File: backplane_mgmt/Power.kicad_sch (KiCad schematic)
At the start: 67 parts, among them J304 VIn, Q301 SUD19P06-60, Q302 SUD19P06-60, U301 AZ1117CD-5.0, U302 PTH08T220, U303 INA209, U304 INA209, U305 AT30TS74

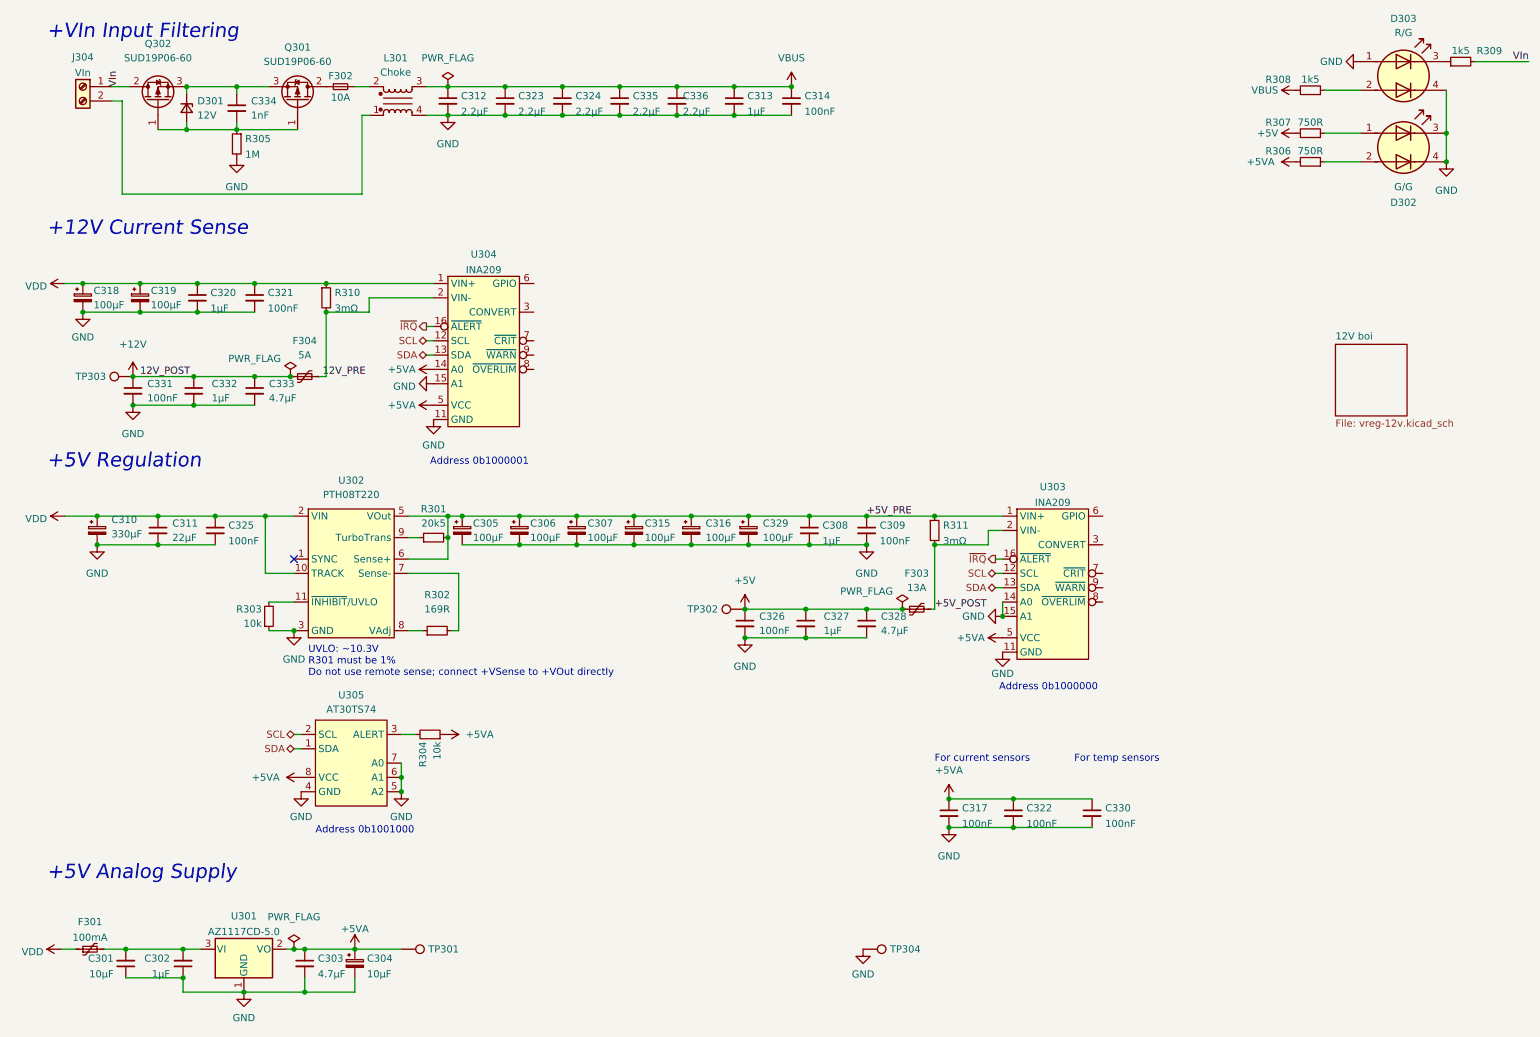
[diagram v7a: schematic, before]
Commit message: Minor layout tweaks across the board
- Added an input for a test clock, and a jumper for sending this clock
  instead of the CPU clock to the clock pins of the expansion cards on
  the backplane boards

- Reworked a bunch of the power supply board

- Minor changes (to consolidate BOMs) on CPU board for some capacitors,
  they were replaced with SMD versions
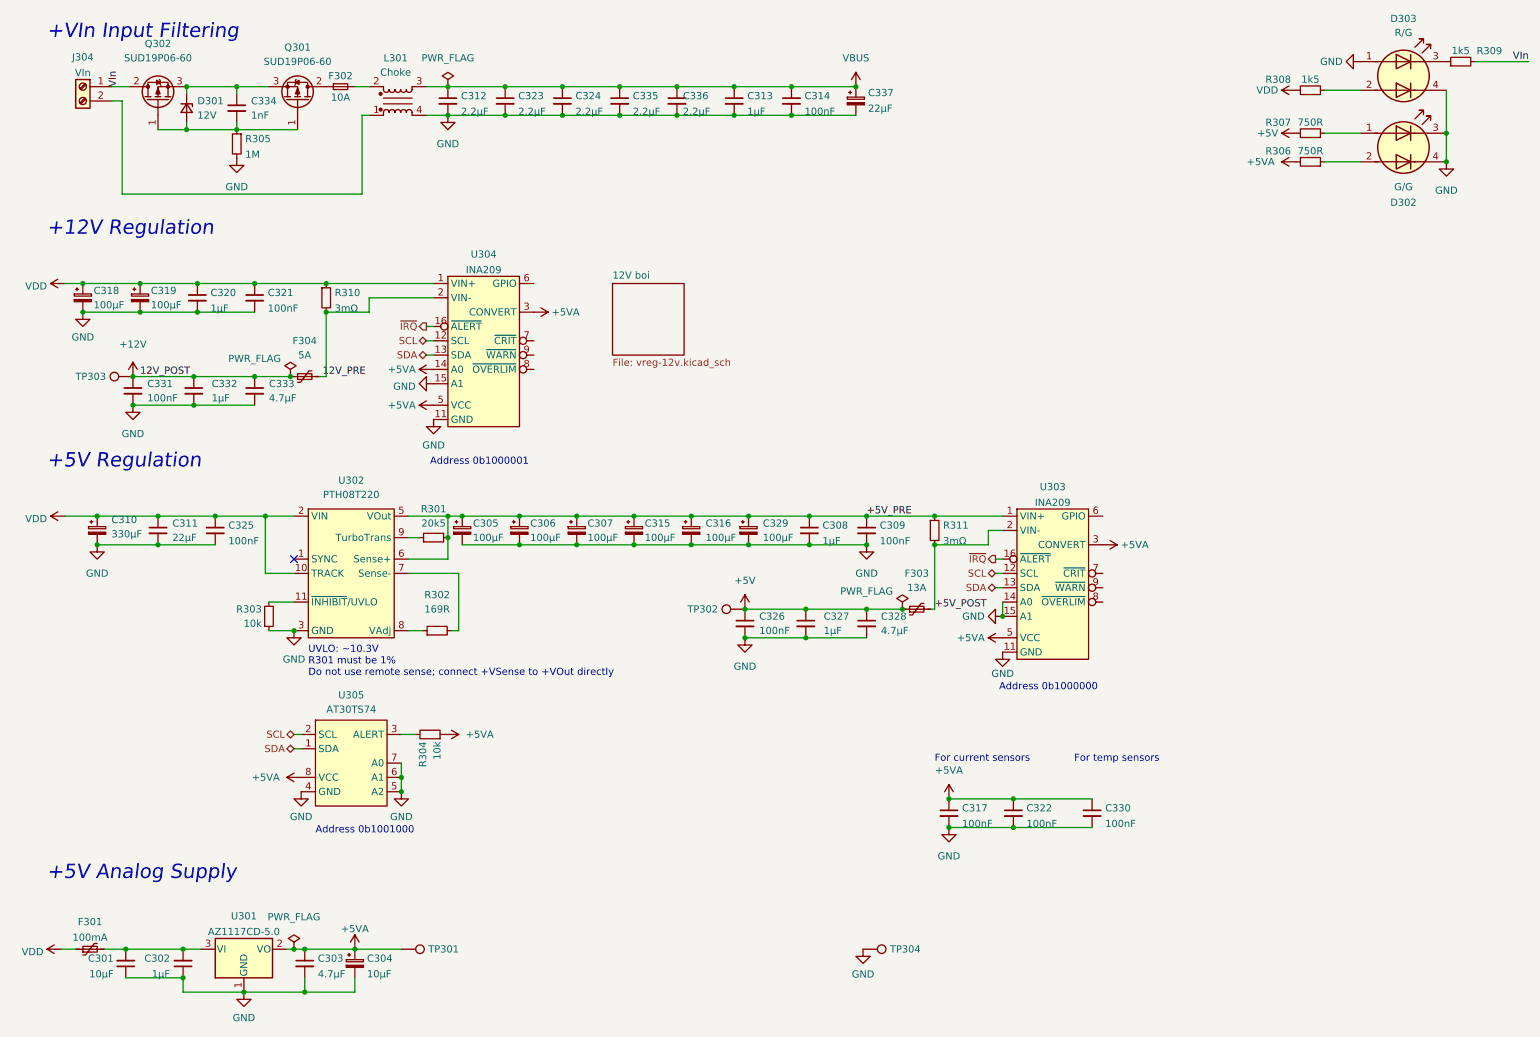
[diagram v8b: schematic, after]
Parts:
- added C337: 22µF, Capacitor_THT:CP_Radial_D5.0mm_P2.00mm, symbol Device:C_Polarized_Small
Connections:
- net +5VA: now also U303.3 (CONVERT), U304.3 (CONVERT)
- net GND: now also C337.2
- net VBUS: now also C337.1; no longer R308.2
- net VDD: now also R308.2
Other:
- note added: "+12V Regulation"
- note removed: "+12V Current Sense"
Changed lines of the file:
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@@
   (junction (at 99.695 31.75) (diameter 0) (color 0 0 0 0)
   )
+  (junction (at 150.495 31.75) (diameter 0) (color 0 0 0 0)
+  )
   (junction (at 27.305 102.87) (diameter 0) (color 0 0 0 0)
   )
@@
   )
   (junction (at 175.895 107.95) (diameter 0) (color 0 0 0 0)
+  )
+  (junction (at 161.925 26.67) (diameter 0) (color 0 0 0 0)
   )
   (junction (at 62.23 179.705) (diameter 0) (color 0 0 0 0)
@@
     (stroke (width 0) (type default) (color 0 0 0 0))
   )
+  (wire (pts (xy 150.495 26.67) (xy 161.925 26.67))
+    (stroke (width 0) (type default) (color 0 0 0 0))
+  )
   (wire (pts (xy 57.15 113.03) (xy 57.15 102.87))
     (stroke (width 0) (type default) (color 0 0 0 0))
@@
   )
   (wire (pts (xy 82.55 123.19) (xy 85.09 123.19))
+    (stroke (width 0) (type default) (color 0 0 0 0))
+  )
+  (wire (pts (xy 150.495 31.75) (xy 161.925 31.75))
     (stroke (width 0) (type default) (color 0 0 0 0))
   )
@@
     (effects (font (size 1.27 1.27)) (justify left bottom))
   )
-  (text "+12V Current Sense" (at 18.415 53.34 0)
+  (text "+12V Regulation" (at 18.415 53.34 0)
     (effects (font (size 2.54 2.54) italic) (justify left bottom))
   )
@@
     (pin "1")
   )
-  (symbol (lib_id "power:VBUS") (at 150.495 26.67 0) (unit 1)
-    (in_bom yes) (on_board yes) (fields_autoplaced)
-    (property "Reference" "#PWR0309" (id 0) (at 150.495 30.48 0)
-      (effects (font (size 1.27 1.27)) hide)
-    )
-    (property "Value" "VBUS" (id 1) (at 150.495 21.59 0))
-    (property "Footprint" "" (id 2) (at 150.495 26.67 0)
-      (effects (font (size 1.27 1.27)) hide)
-    )
-    (property "Datasheet" "" (id 3) (at 150.495 26.67 0)
+  (symbol (lib_id "power:VBUS") (at 161.925 26.67 0) (unit 1)
+    (in_bom yes) (on_board yes) (fields_autoplaced)
+    (property "Reference" "#PWR0309" (id 0) (at 161.925 30.48 0)
+      (effects (font (size 1.27 1.27)) hide)
+    )
+    (property "Value" "VBUS" (id 1) (at 161.925 21.59 0))
+    (property "Footprint" "" (id 2) (at 161.925 26.67 0)
+      (effects (font (size 1.27 1.27)) hide)
+    )
+    (property "Datasheet" "" (id 3) (at 161.925 26.67 0)
       (effects (font (size 1.27 1.27)) hide)
     )
@@
     (pin "2")
   )
+  (symbol (lib_id "power:VDD") (at 240.03 27.305 90) (unit 1)
+    (in_bom yes) (on_board yes)
+    (property "Reference" "#PWR0118" (id 0) (at 243.84 27.305 0)
+      (effects (font (size 1.27 1.27)) hide)
+    )
+    (property "Value" "VDD" (id 1) (at 236.855 27.305 90)
+      (effects (font (size 1.27 1.27)) (justify left))
+    )
+    (property "Footprint" "" (id 2) (at 240.03 27.305 0)
+      (effects (font (size 1.27 1.27)) hide)
+    )
+    (property "Datasheet" "" (id 3) (at 240.03 27.305 0)
+      (effects (font (size 1.27 1.27)) hide)
+    )
+    (pin "1")
+  )
   (symbol (lib_id "power:VDD") (at 21.59 102.87 90) (unit 1)
     (in_bom yes) (on_board yes) (fields_autoplaced)
@@
     )
     (property "MPN" "LRMAP2512-R003FT4" (id 4) (at 67.945 64.135 0)
+      (effects (font (size 1.27 1.27)) hide)
+    )
+    (pin "1")
+    (pin "2")
+  )
+  (symbol (lib_id "Device:C_Polarized_Small") (at 161.925 29.21 0) (unit 1)
+    (in_bom yes) (on_board yes) (fields_autoplaced)
+    (property "Reference" "C337" (id 0) (at 164.084 27.7554 0)
+      (effects (font (size 1.27 1.27)) (justify left))
+    )
+    (property "Value" "22µF" (id 1) (at 164.084 30.5305 0)
+      (effects (font (size 1.27 1.27)) (justify left))
+    )
+    (property "Footprint" "Capacitor_THT:CP_Radial_D5.0mm_P2.00mm" (id 2) (at 161.925 29.21 0)
+      (effects (font (size 1.27 1.27)) hide)
+    )
+    (property "Datasheet" "~" (id 3) (at 161.925 29.21 0)
       (effects (font (size 1.27 1.27)) hide)
     )
@@
     (pin "2")
   )
-  (symbol (lib_id "power:VBUS") (at 240.03 27.305 90) (unit 1)
-    (in_bom yes) (on_board yes) (fields_autoplaced)
-    (property "Reference" "#PWR0335" (id 0) (at 243.84 27.305 0)
-      (effects (font (size 1.27 1.27)) hide)
-    )
-    (property "Value" "VBUS" (id 1) (at 236.855 27.3049 90)
-      (effects (font (size 1.27 1.27)) (justify left))
-    )
-    (property "Footprint" "" (id 2) (at 240.03 27.305 0)
-      (effects (font (size 1.27 1.27)) hide)
-    )
-    (property "Datasheet" "" (id 3) (at 240.03 27.305 0)
+  (symbol (lib_id "power:+5VA") (at 104.775 66.675 270) (unit 1)
+    (in_bom yes) (on_board yes)
+    (property "Reference" "#PWR0117" (id 0) (at 100.965 66.675 0)
+      (effects (font (size 1.27 1.27)) hide)
+    )
+    (property "Value" "+5VA" (id 1) (at 107.95 66.675 90)
+      (effects (font (size 1.27 1.27)) (justify left))
+    )
+    (property "Footprint" "" (id 2) (at 104.775 66.675 0)
+      (effects (font (size 1.27 1.27)) hide)
+    )
+    (property "Datasheet" "" (id 3) (at 104.775 66.675 0)
       (effects (font (size 1.27 1.27)) hide)
     )
@@
     (pin "1")
     (pin "2")
+  )
+  (symbol (lib_id "power:+5VA") (at 205.74 107.95 270) (unit 1)
+    (in_bom yes) (on_board yes)
+    (property "Reference" "#PWR0116" (id 0) (at 201.93 107.95 0)
+      (effects (font (size 1.27 1.27)) hide)
+    )
+    (property "Value" "+5VA" (id 1) (at 208.915 107.95 90)
+      (effects (font (size 1.27 1.27)) (justify left))
+    )
+    (property "Footprint" "" (id 2) (at 205.74 107.95 0)
+      (effects (font (size 1.27 1.27)) hide)
+    )
+    (property "Datasheet" "" (id 3) (at 205.74 107.95 0)
+      (effects (font (size 1.27 1.27)) hide)
+    )
+    (pin "1")
   )
   (symbol (lib_id "Device:C_Small") (at 99.695 29.21 0) (unit 1)
@@
     (pin "4")
   )
-  (sheet (at 247.015 72.39) (size 12.7 12.7) (fields_autoplaced)
+  (sheet (at 118.745 61.595) (size 12.7 12.7) (fields_autoplaced)
     (stroke (width 0.1524) (type solid) (color 0 0 0 0))
     (fill (color 0 0 0 0.0000))
-    (property "Sheet name" "12V boi" (id 0) (at 247.015 71.6784 0)
+    (property "Sheet name" "12V boi" (id 0) (at 118.745 60.8834 0)
       (effects (font (size 1.27 1.27)) (justify left bottom))
     )
-    (property "Sheet file" "vreg-12v.kicad_sch" (id 1) (at 247.015 85.6746 0)
+    (property "Sheet file" "vreg-12v.kicad_sch" (id 1) (at 118.745 74.8796 0)
       (effects (font (size 1.27 1.27)) (justify left top))
     )
